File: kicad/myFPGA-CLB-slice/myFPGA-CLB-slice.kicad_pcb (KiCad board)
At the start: 2 copper layers, 100 x 140 mm, 157 parts, among them J1 Conn_01x04, J10 Conn_01x02, J11 Conn_01x02, J12 Conn_01x04, J13 Conn_01x04, J14 Conn_01x04, J15 Conn_01x04, J2 Conn_01x04, J3 Conn_01x04, J4 Conn_01x04, J5 Conn_01x04, J6 Conn_01x04, J7 Conn_01x04, J8 Conn_01x02, J9 Conn_01x04, U1 NC7SB3157P6X, U10 NC7SB3157P6X, U11 NC7SB3157P6X, U12 NC7SB3157P6X, U13 74LS157, U14 NC7SB3157P6X, U15 NC7SB3157P6X, U16 NC7SB3157P6X, U17 NC7SB3157P6X, U18 74LS175, U19 74AHCT595, U2 74AHCT595, U20 74AHCT595, U21 74LS151, U22 74LS151, U23 NC7SB3157P6X, U24 74AHCT595, U25 74AHCT595, U26 74LS151, U27 74LS151, U28 NC7SB3157P6X, U29 74AHCT595, U3 74AHCT595, U30 74AHCT595, U31 74LS151, U32 74LS151, U33 NC7SB3157P6X, U34 74LS153, U35 74LS153, U36 74LS153, U37 74LS153, U38 74AHCT595, U4 74AHCT595, U5 74LS151, U6 74LS151, U7 NC7SB3157P6X, U8 74HC86, U9 NC7SB3157P6X

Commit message: SWbox layout nearly complete
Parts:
- moved J2 1.00 mm to (54.0, 54.0)
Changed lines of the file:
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@@
   )
   (footprint "Connector_PinHeader_2.54mm:PinHeader_1x04_P2.54mm_Horizontal" locked (layer "F.Cu")
-    (at 55 54 180)
+    (at 54 54 180)
     (descr "Through hole angled pin header, 1x04, 2.54mm pitch, 6mm pin length, single row")
     (tags "Through hole angled pin header THT 1x04 2.54mm single row")
@@
   (gr_line (start 54 30) (end 54 170)
     (stroke (width 0.15) (type default)) (layer "Dwgs.User"))
-  (gr_line (start 55 30) (end 55 54)
-    (stroke (width 0.15) (type default)) (layer "Dwgs.User"))
   (gr_line (start 40 100) (end 150 100)
     (stroke (width 0.15) (type default)) (layer "Dwgs.User"))
-  (gr_line (start 55 54) (end 55 66)
-    (stroke (width 0.15) (type default)) (layer "Dwgs.User"))
   (gr_line (start 89 170) (end 89 28)

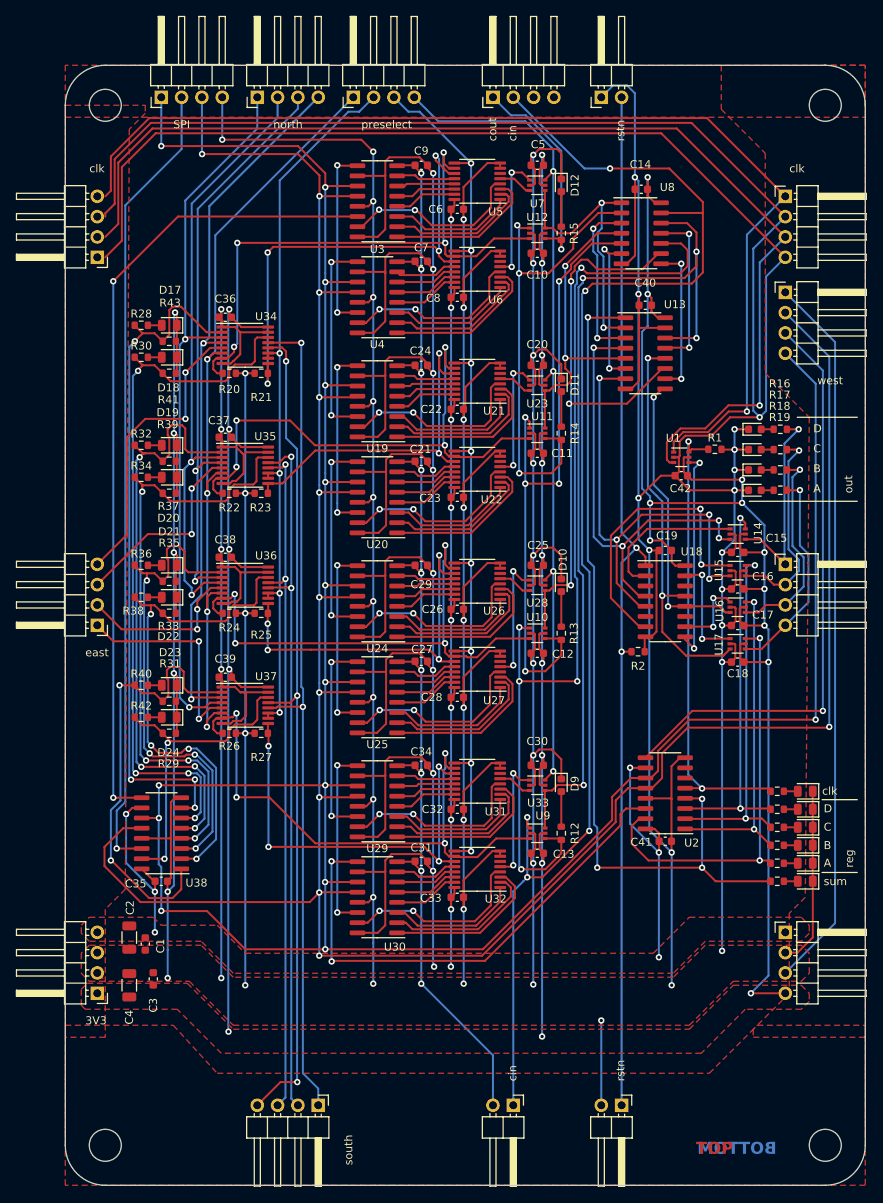
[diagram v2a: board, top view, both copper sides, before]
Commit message: CLB requires rev.2
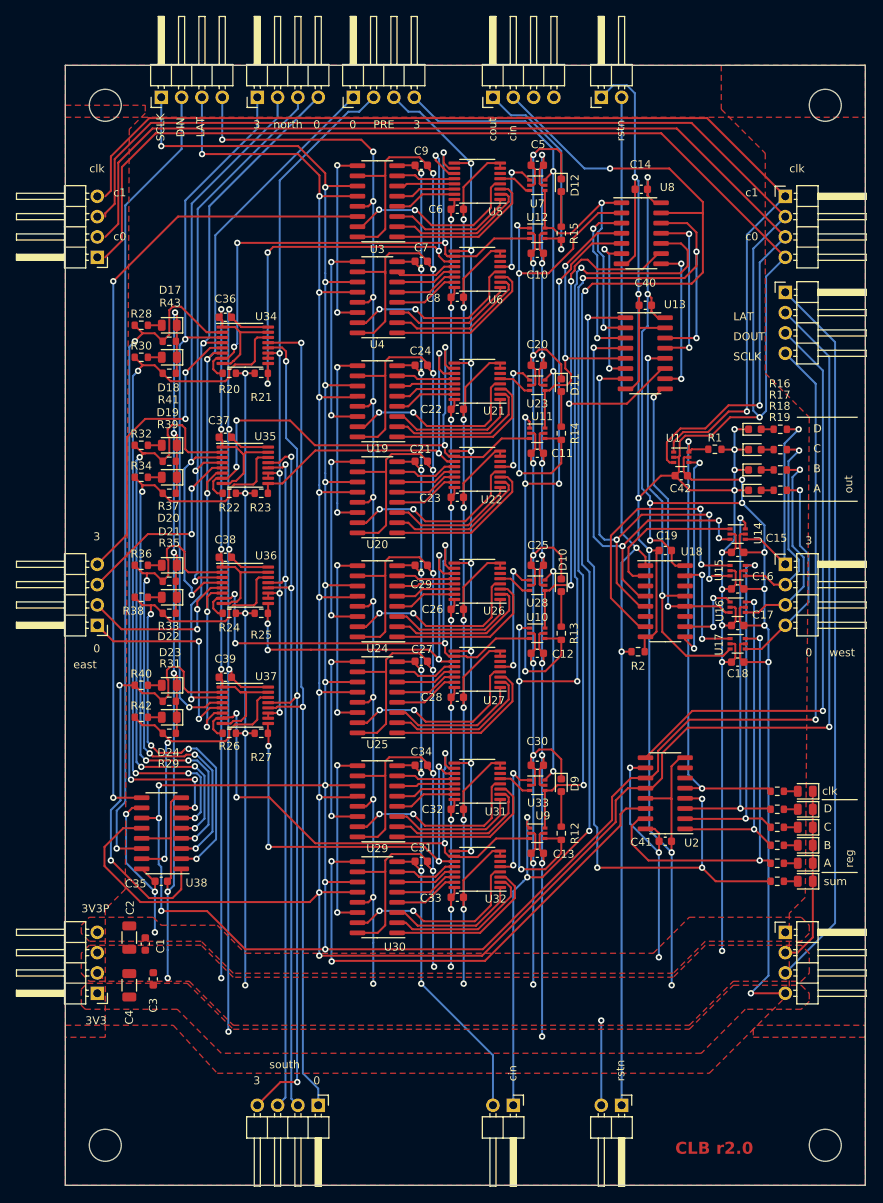
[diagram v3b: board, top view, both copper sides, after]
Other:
- outline, holes or cut-outs redrawn
- board text added: "0"
- board text added: "3"
- board text added: "3V3P"
- board text added: "CLB r2.0"
- board text added: "DIN"
- board text added: "DOUT"
- board text added: "LAT"
- board text added: "PRE"
- board text added: "SCLK"
- board text added: "c0"
- board text added: "c1"
- board text removed: "BOTTOM"
- board text removed: "SPI"
- board text removed: "TOP"
- board text removed: "preselect"
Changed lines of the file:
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@@
   (gr_line (start 90 109) (end 88 109)
     (stroke (width 0.15) (type default)) (layer "Cmts.User"))
-  (gr_arc (start 50 35) (mid 51.464466 31.464466) (end 55 30)
-    (stroke (width 0.1) (type default)) (layer "Edge.Cuts"))
-  (gr_arc (start 55 170) (mid 51.464466 168.535534) (end 50 165)
-    (stroke (width 0.1) (type default)) (layer "Edge.Cuts"))
   (gr_circle (center 145 35) (end 147 35)
     (stroke (width 0.1) (type default)) (fill none) (layer "Edge.Cuts"))
-  (gr_line (start 150 165) (end 150 35)
+  (gr_line (start 150 170) (end 150 30)
     (stroke (width 0.1) (type default)) (layer "Edge.Cuts"))
-  (gr_arc (start 145 30) (mid 148.535534 31.464466) (end 150 35)
-    (stroke (width 0.1) (type default)) (layer "Edge.Cuts"))
-  (gr_line (start 50 35) (end 50 165)
+  (gr_line (start 50 30) (end 50 170)
     (stroke (width 0.1) (type default)) (layer "Edge.Cuts"))
   (gr_circle (center 145 165) (end 145 167)
     (stroke (width 0.1) (type default)) (fill none) (layer "Edge.Cuts"))
-  (gr_line (start 55 170) (end 145 170)
+  (gr_line (start 50 170) (end 150 170)
     (stroke (width 0.1) (type default)) (layer "Edge.Cuts"))
-  (gr_line (start 145 30) (end 55 30)
+  (gr_line (start 150 30) (end 50 30)
     (stroke (width 0.1) (type default)) (layer "Edge.Cuts"))
   (gr_circle (center 55 35) (end 57 35)
@@
   (gr_circle (center 55 165) (end 53 165)
     (stroke (width 0.1) (type default)) (fill none) (layer "Edge.Cuts"))
-  (gr_arc (start 150 165) (mid 148.535534 168.535534) (end 145 170)
-    (stroke (width 0.1) (type default)) (layer "Edge.Cuts"))
-  (gr_text "TOP" (at 133.5 166.25) (layer "F.Cu")
+  (gr_text "CLB r2.0" (at 136 166.25) (layer "F.Cu")
     (effects (font (size 1.5 1.5) (thickness 0.3) bold) (justify right bottom))
   )
-  (gr_text "BOTTOM" (at 129 166.25) (layer "B.Cu")
-    (effects (font (size 1.5 1.5) (thickness 0.3) bold) (justify right bottom mirror))
+  (gr_text "A" (at 143.5 83.5) (layer "F.SilkS")
+    (effects (font (size 1 1) (thickness 0.15)) (justify left bottom))
   )
-  (gr_text "A" (at 143.5 83.5) (layer "F.SilkS")
+  (gr_text "0" (at 53.5 103.5) (layer "F.SilkS")
     (effects (font (size 1 1) (thickness 0.15)) (justify left bottom))
   )
@@
     (effects (font (size 1 1) (thickness 0.15)) (justify left bottom))
   )
-  (gr_text "east" (at 52.5 104) (layer "F.SilkS")
+  (gr_text "0" (at 81 38) (layer "F.SilkS")
+    (effects (font (size 1 1) (thickness 0.15)) (justify left bottom))
+  )
+  (gr_text "east" (at 51 105.5) (layer "F.SilkS")
+    (effects (font (size 1 1) (thickness 0.15)) (justify left bottom))
+  )
+  (gr_text "DIN" (at 65 39 90) (layer "F.SilkS")
     (effects (font (size 1 1) (thickness 0.15)) (justify left bottom))
   )
   (gr_text "north" (at 76 38) (layer "F.SilkS")
+    (effects (font (size 1 1) (thickness 0.15)) (justify left bottom))
+  )
+  (gr_text "3" (at 93.5 38) (layer "F.SilkS")
+    (effects (font (size 1 1) (thickness 0.15)) (justify left bottom))
+  )
+  (gr_text "0" (at 142.5 104) (layer "F.SilkS")
+    (effects (font (size 1 1) (thickness 0.15)) (justify left bottom))
+  )
+  (gr_text "c1" (at 56 46.5) (layer "F.SilkS")
+    (effects (font (size 1 1) (thickness 0.15)) (justify left bottom))
+  )
+  (gr_text "SCLK" (at 62.5 39.5 90) (layer "F.SilkS")
+    (effects (font (size 1 1) (thickness 0.15)) (justify left bottom))
+  )
+  (gr_text "LAT" (at 133.5 62) (layer "F.SilkS")
     (effects (font (size 1 1) (thickness 0.15)) (justify left bottom))
   )
@@
     (effects (font (size 1 1) (thickness 0.15)) (justify left bottom))
   )
-  (gr_text "SPI" (at 63.5 38) (layer "F.SilkS")
+  (gr_text "0" (at 81 157.5) (layer "F.SilkS")
     (effects (font (size 1 1) (thickness 0.15)) (justify left bottom))
   )
-  (gr_text "west" (at 144 70) (layer "F.SilkS")
+  (gr_text "west" (at 145.5 104) (layer "F.SilkS")
     (effects (font (size 1 1) (thickness 0.15)) (justify left bottom))
   )
@@
     (effects (font (size 1 1) (thickness 0.15)) (justify left bottom))
   )
+  (gr_text "0" (at 85.5 38) (layer "F.SilkS")
+    (effects (font (size 1 1) (thickness 0.15)) (justify left bottom))
+  )
   (gr_text "D" (at 143.5 76) (layer "F.SilkS")
+    (effects (font (size 1 1) (thickness 0.15)) (justify left bottom))
+  )
+  (gr_text "c0" (at 135 52) (layer "F.SilkS")
+    (effects (font (size 1 1) (thickness 0.15)) (justify left bottom))
+  )
+  (gr_text "DOUT" (at 133.5 64.5) (layer "F.SilkS")
     (effects (font (size 1 1) (thickness 0.15)) (justify left bottom))
   )
@@
     (effects (font (size 1 1) (thickness 0.15)) (justify left bottom))
   )
+  (gr_text "3" (at 53.5 89.5) (layer "F.SilkS")
+    (effects (font (size 1 1) (thickness 0.15)) (justify left bottom))
+  )
+  (gr_text "SCLK" (at 133.5 67) (layer "F.SilkS")
+    (effects (font (size 1 1) (thickness 0.15)) (justify left bottom))
+  )
+  (gr_text "3" (at 73.5 38) (layer "F.SilkS")
+    (effects (font (size 1 1) (thickness 0.15)) (justify left bottom))
+  )
+  (gr_text "3" (at 142.5 90) (layer "F.SilkS")
+    (effects (font (size 1 1) (thickness 0.15)) (justify left bottom))
+  )
   (gr_text "A" (at 144.8 130.3) (layer "F.SilkS")
     (effects (font (size 1 1) (thickness 0.15)) (justify left bottom))
@@
     (effects (font (size 1 1) (thickness 0.15)) (justify left bottom))
   )
+  (gr_text "3V3P" (at 52 136) (layer "F.SilkS")
+    (effects (font (size 1 1) (thickness 0.15)) (justify left bottom))
+  )
   (gr_text "reg" (at 148.6 130.3 90) (layer "F.SilkS")
+    (effects (font (size 1 1) (thickness 0.15)) (justify left bottom))
+  )
+  (gr_text "c1" (at 135 46.5) (layer "F.SilkS")
     (effects (font (size 1 1) (thickness 0.15)) (justify left bottom))
   )
@@
     (effects (font (size 1 1) (thickness 0.15)) (justify left bottom))
   )
+  (gr_text "LAT" (at 67.5 39 90) (layer "F.SilkS")
+    (effects (font (size 1 1) (thickness 0.15)) (justify left bottom))
+  )
   (gr_text "3V3" (at 52.5 150) (layer "F.SilkS")
     (effects (font (size 1 1) (thickness 0.15)) (justify left bottom))
   )
-  (gr_text "south" (at 86 167.5 90) (layer "F.SilkS")
+  (gr_text "south" (at 75.5 155.5) (layer "F.SilkS")
     (effects (font (size 1 1) (thickness 0.15)) (justify left bottom))
   )
-  (gr_text "preselect" (at 87 38) (layer "F.SilkS")
+  (gr_text "PRE" (at 88.5 38) (layer "F.SilkS")
     (effects (font (size 1 1) (thickness 0.15)) (justify left bottom))
   )
+  (gr_text "3" (at 73.5 157.5) (layer "F.SilkS")
+    (effects (font (size 1 1) (thickness 0.15)) (justify left bottom))
+  )
+  (gr_text "c0" (at 56 52) (layer "F.SilkS")
+    (effects (font (size 1 1) (thickness 0.15)) (justify left bottom))
+  )

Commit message: CLB slice rev. 2.0 - fix aresetn pullup instead of pulldown - new feature: clock enable - fixes S0 and S1 flipped
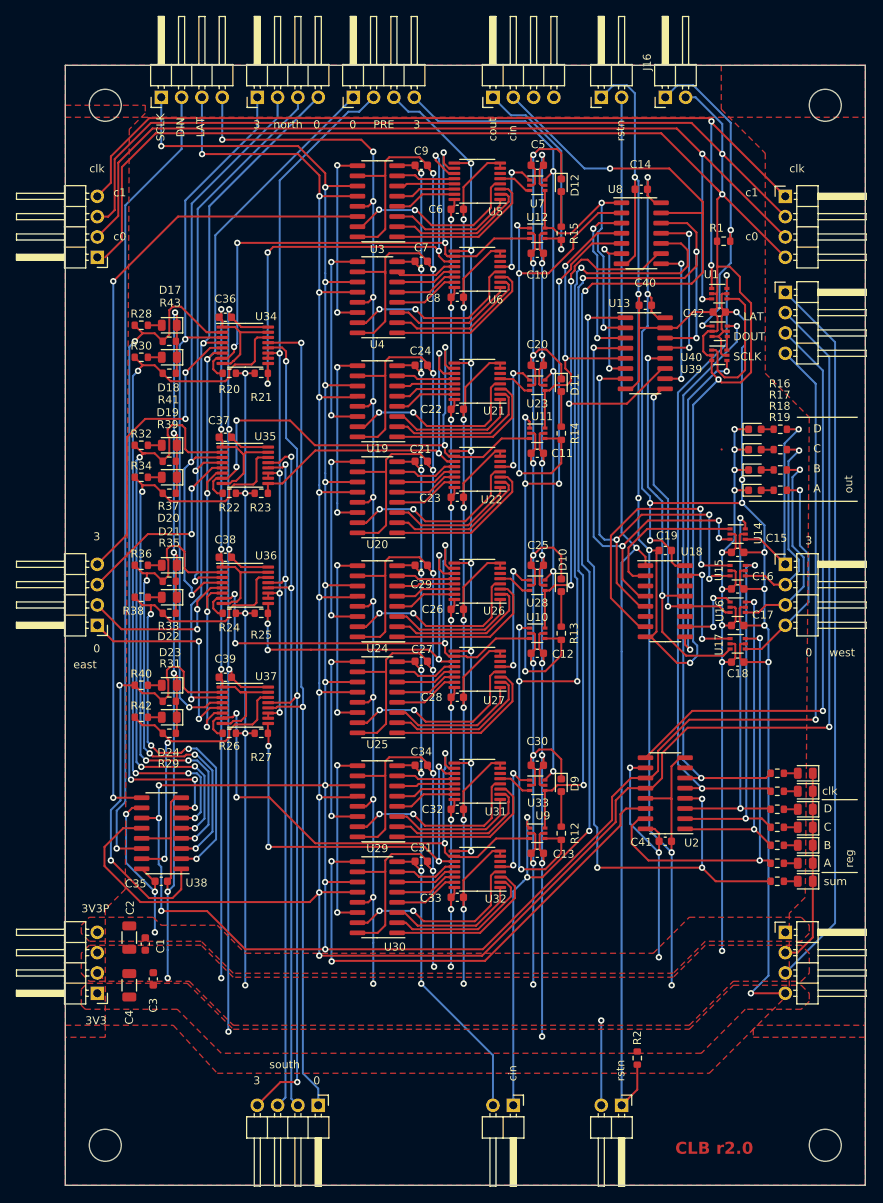
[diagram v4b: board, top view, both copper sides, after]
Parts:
- added D1: LED (green), LED_SMD:LED_0805_2012Metric, F.Cu at (142.5, 118.5)
- added J16: Conn_01x02, Connector_PinHeader_2.54mm:PinHeader_1x02_P2.54mm_Horizontal, F.Cu at (125.0, 34.0)
- added R3: 330R, Resistor_SMD:R_0603_1608Metric, F.Cu at (139.0, 118.5)
- added U39: NC7SB3157P6X, Package_TO_SOT_SMD:SOT-363_SC-70-6, F.Cu at (131.8, 66.2)
- added U40: NC7SB3157P6X, Package_TO_SOT_SMD:SOT-363_SC-70-6, F.Cu at (131.8, 63.2)
- moved R2 50.8 mm to (121.5, 154.1), turned to 90 degrees
- moved R1 26.0 mm to (132.3, 52.0), turned to 180 degrees
- moved U1 21.0 mm to (131.8, 58.5)
- moved C42 21.0 mm to (131.8, 60.9)
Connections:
- R1 pad 1: set_clk_sel -> /ext_ce
- R2 pad 2: GND -> +3V3
- U1 pad 4: latch_clk -> /clk_s
- U2 pad 6: unconnected-(U2-QG-Pad6) -> set_ce
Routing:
- net set_ce: track 0.00 -> 72.3 mm, vias 0 -> 2
- net /ext_ce: track 0.00 -> 40.2 mm, vias 0 -> 2
- net GND: track 1676.4 -> 1712.3 mm, vias 71 -> 74
- net +3V3: track 439.4 -> 463.2 mm, vias 25 -> 26
- net set_clk_sel: track 58.9 -> 80.4 mm
- net /clk_1: track 136.5 -> 117.0 mm, vias 1 -> 2
- net /clk_0: track 139.8 -> 120.5 mm, vias 1 -> 2
- net /clk_s: track 0.00 -> 18.0 mm
- net latch_clk: track 26.8 -> 40.9 mm
- net aresetn: track 131.5 -> 136.2 mm, vias 2 -> 1
- net Net-(D1-A): track 0.00 -> 1.74 mm
- net /ce: track 0.00 -> 1.72 mm
